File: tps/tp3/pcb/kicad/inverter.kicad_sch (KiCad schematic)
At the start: 100 parts, among them J1 220Vac In, J2 Motor, J3 5Vext In, J4 Conn_01x03_Pin, J5 Conn_01x03_Pin, J6 15Vext In, J7 Vd out, J8 Conn_01x03_Pin, Q1 IRF820, Q2 IRF820, Q3 IRF820, Q4 IRF820, Q5 IRF820, Q6 IRF820, U1 IR2110-A, U2 IR2110-B, U3 IR2110-C, U4 ESP32-DEVKIT-V1

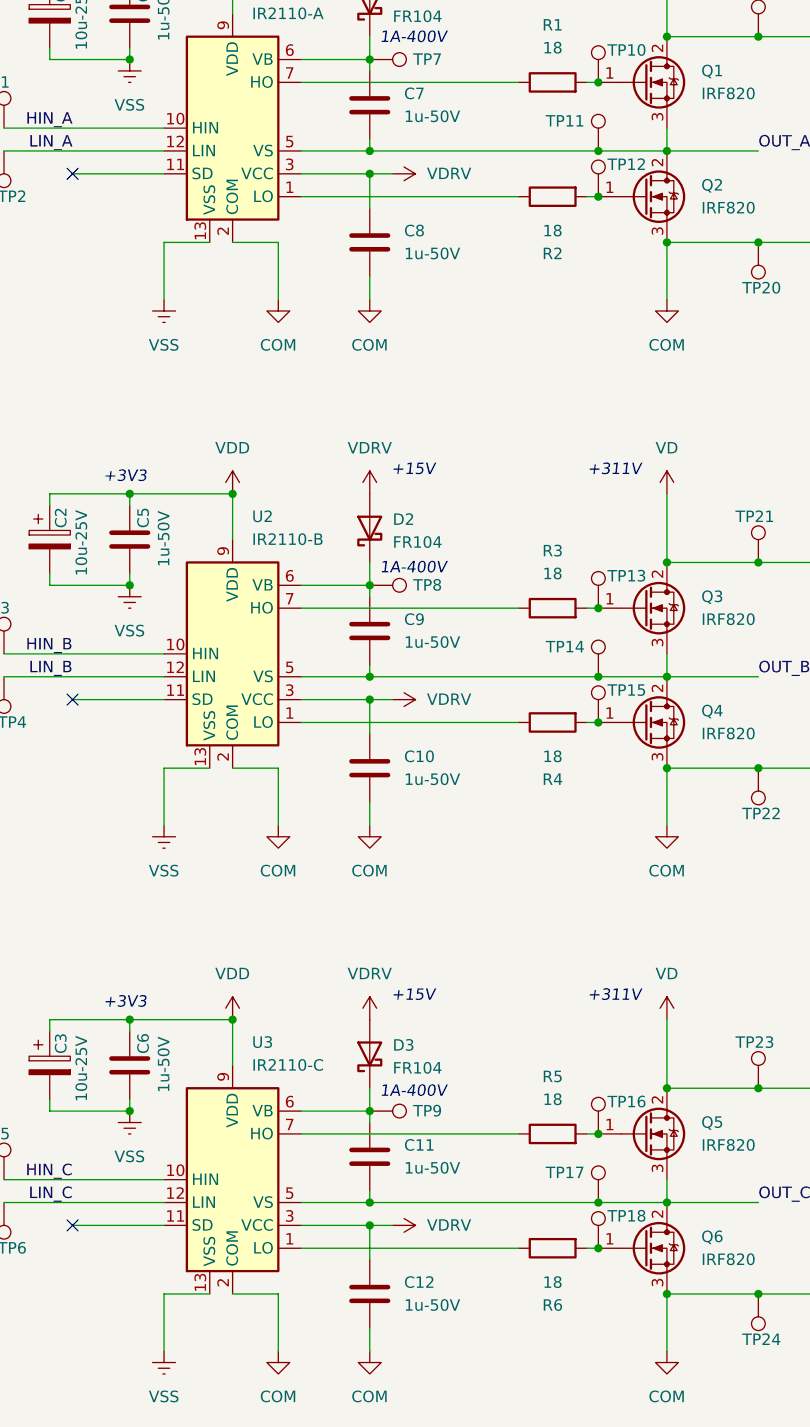
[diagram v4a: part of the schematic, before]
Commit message: add more 15V decoupling caps, update exported sch, add potentiometer 3D model, some routing progress
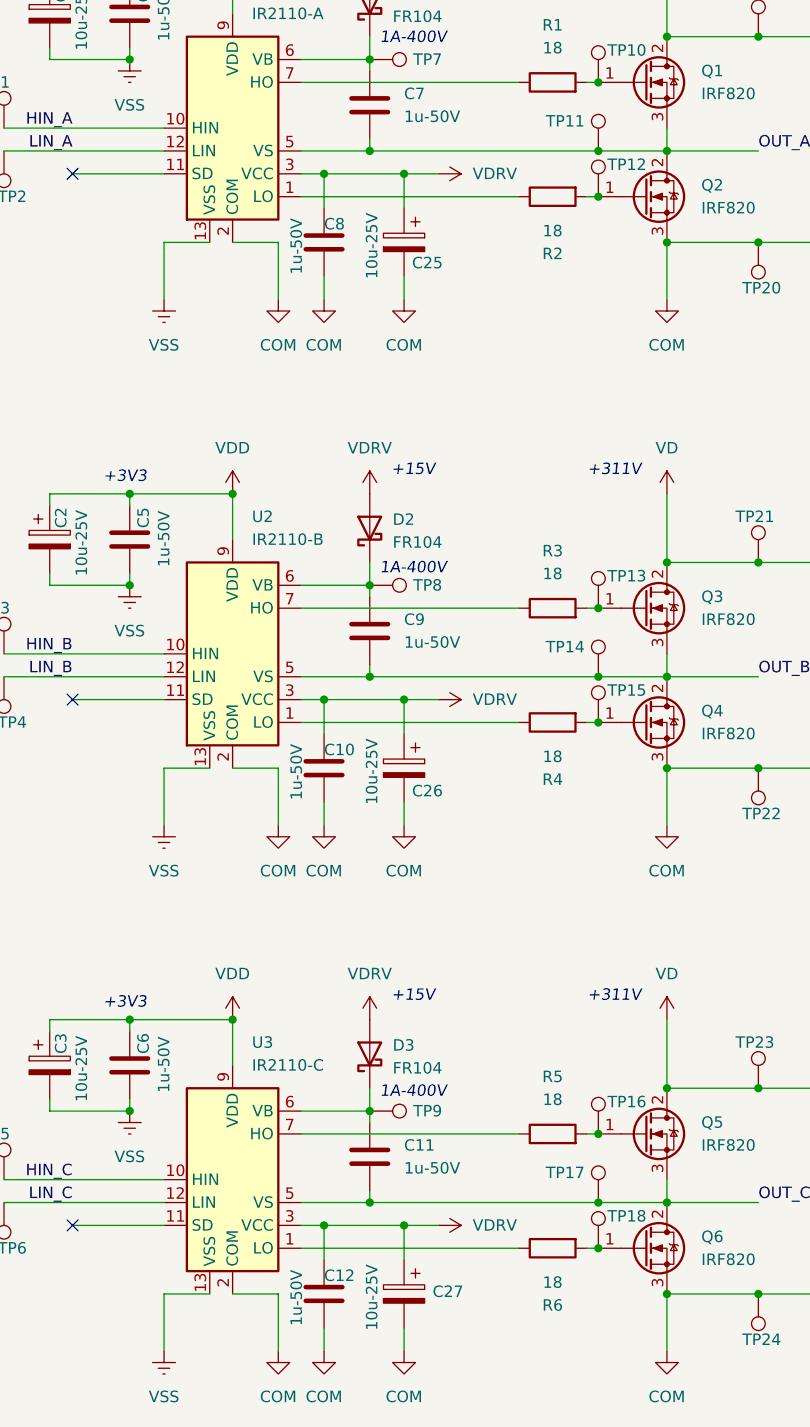
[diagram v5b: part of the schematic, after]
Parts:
- added C25, C26, C27: 10u-25V, Capacitor_THT:CP_Radial_D4.0mm_P1.50mm, symbol Device:C_Polarized
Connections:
- net COM: now also C25.2, C26.2, C27.2
- net VDRV: now also C25.1, C26.1, C27.1
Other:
- moved on the sheet: C8

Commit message: avances pcb
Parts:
- added C28, C29, C30: 10u-25V, Capacitor_THT:CP_Radial_D4.0mm_P1.50mm, symbol Device:C_Polarized
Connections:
- net HIN_A: now also R10.1; no longer R9.1
- net HIN_B: now also R12.1; no longer R11.1
- net HIN_C: now also R14.1; no longer R13.1
- net LIN_A: now also R9.1; no longer R10.1
- net LIN_B: now also R11.1; no longer R12.1
- net LIN_C: now also R13.1; no longer R14.1
- net OUT_A: now also C28.2
- net OUT_B: now also C29.2
- net OUT_C: now also C30.2
- net at R13.2: now also U4.7 (TX2); no longer U4.10 (D19)
- net at R10.2: now also U4.4 (D2); no longer U4.26 (D14)
- net at C7.1, D1.1 (K), TP7.1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: now also C28.1
- net at RV1.2, TP29.1: now also U4.19 (D34); no longer U4.25 (D27)
- net at R11.2: now also U4.5 (D4); no longer U4.3 (D15)
- net at C11.1, D3.1 (K), TP9.1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: now also C30.1
- net at C9.1, D2.1 (K), TP8.1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: now also C29.1
- net at J8.1 (Pin_1): now also U4.25 (D27); no longer U4.19 (D34)
- net at J8.2 (Pin_2): now also U4.24 (D26); no longer U4.20 (D35)
- net at J8.3 (Pin_3): now also U4.23 (D25); no longer U4.22 (D33)
- net at R9.2: now also U4.3 (D15); no longer U4.28 (D13)
- net at R14.2: now also U4.8 (D5); no longer U4.11 (D21)
- net at R12.2: now also U4.6 (RX2); no longer U4.9 (D18)
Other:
- note added: "ADC1_6"
- note added: "D16"
- note added: "D17"
- note removed: "ADC2_7"
- moved on the sheet: C11, C13, C14, C15, C7, C9, J8, Q1, Q2, Q3, Q4, Q5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
